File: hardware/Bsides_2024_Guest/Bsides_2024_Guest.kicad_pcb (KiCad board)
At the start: 2 copper layers, 134.5 x 129.5 mm, 53 parts, among them J1 Add_On, J2 Battery, J3 Battery, J4 OLED, J5 Serial_IN, J6 Serial_OUT, P1 USB_C_Plug_USB2.0, Q1 DMG3415U-7, SW1 ON, SW2 RESET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

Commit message: feat(Hw): Labels added
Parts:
- added kibuzzard-666B5A62: G***, kibuzzard-666B5A62, F.Cu at (179.3, 143.8)
- added kibuzzard-666B5A62: G***, kibuzzard-666B5A62, B.Cu at (70.0, 137.2)
- added kibuzzard-666B5A91: G***, kibuzzard-666B5A91, F.Cu at (181.1, 142.0)
- added kibuzzard-666B5A91: G***, kibuzzard-666B5A91, B.Cu at (71.7, 138.9)
- added kibuzzard-666B5AA1: G***, kibuzzard-666B5AA1, F.Cu at (182.7, 139.9)
- added kibuzzard-666B5AA1: G***, kibuzzard-666B5AA1, B.Cu at (68.4, 135.1)
- added kibuzzard-666B5BCA: G***, kibuzzard-666B5BCA, B.Cu at (142.8, 70.0)
- added kibuzzard-666B5C0A: G***, kibuzzard-666B5C0A, B.Cu at (142.0, 72.3)
- added kibuzzard-666B5C33: G***, kibuzzard-666B5C33, B.Cu at (144.6, 77.5)
- moved J3 2.95 mm to (115.4, 93.0)
- moved J2 2.79 mm to (132.9, 41.5)
- moved C5 1.26 mm to (104.3, 43.1)
- moved R6 0.25 mm to (102.4, 41.4)
- turned kibuzzard-666B5E08 to 135.5 degrees
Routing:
- net +BATT: track 47.0 -> 49.5 mm
- net GND: track 53.5 -> 55.1 mm
- net /VOUT: track 428.7 -> 429.8 mm
- net /PIN: track 108.3 -> 109.0 mm
- net Net-(D2-DIN): track 2.52 -> 1.98 mm

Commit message: feat(Hw): Update labels
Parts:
- removed kibuzzard-666B5EBB: G***, kibuzzard-666B5EBB
- added kibuzzard-666B5BCA: G***, kibuzzard-666B5BCA, B.Cu at (132.9, 91.0)
- added kibuzzard-666B5BCA: G***, kibuzzard-666B5BCA, B.Cu at (115.4, 43.3)
- added kibuzzard-666B5C0A: G***, kibuzzard-666B5C0A, B.Cu at (132.9, 43.0)
- added kibuzzard-666B5C0A: G***, kibuzzard-666B5C0A, B.Cu at (115.4, 91.2)
- added kibuzzard-666C662F: G***, kibuzzard-666C662F, B.Cu at (88.3, 71.7)

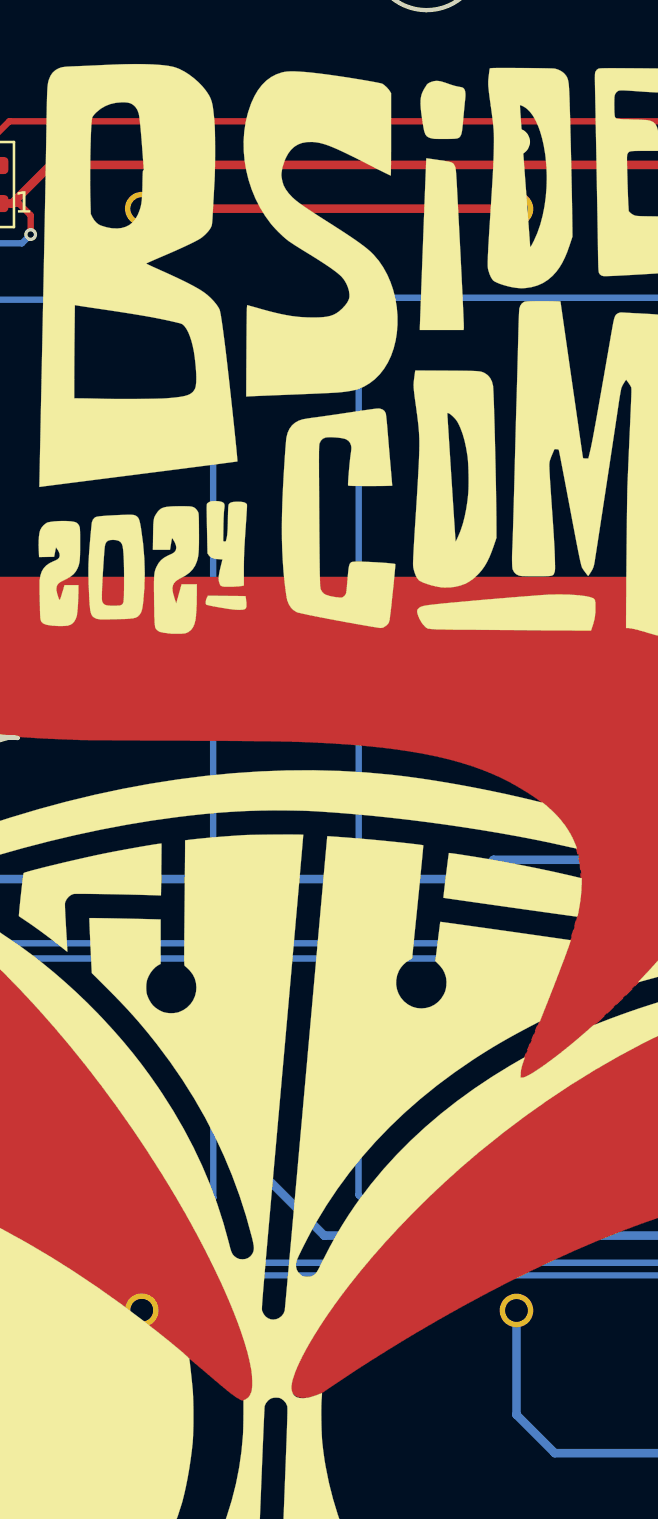
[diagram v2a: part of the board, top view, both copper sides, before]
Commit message: feat(Hw): Update labels
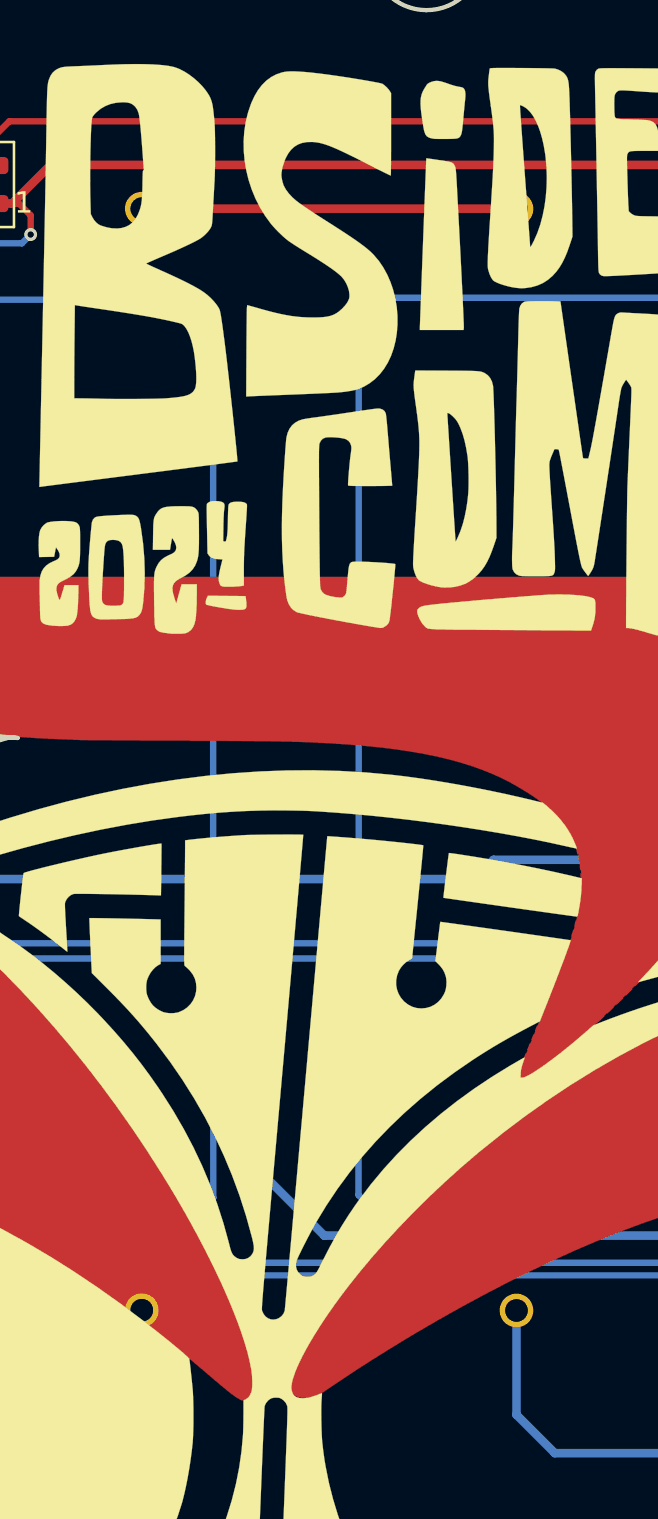
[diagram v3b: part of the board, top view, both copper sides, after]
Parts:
- removed the kibuzzard-666B5BCA at (115.4, 43.3)
- removed the kibuzzard-666B5C0A at (132.9, 43.0)
- moved kibuzzard-666B5BCA 5.99 mm to (132.9, 97.0)
- moved kibuzzard-666B5C0A 5.58 mm to (115.4, 96.7)
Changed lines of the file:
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@@
 		(attr through_hole)
 		(fp_line
-			(start -54.057905 -8.4906)
-			(end -54.057905 8.502)
+			(start 2.507895 -8.4906)
+			(end -54.057905 -8.4906)
 			(stroke
 				(width 0.1524)
@@
 		)
 		(fp_line
-			(start 2.507895 -8.490599)
-			(end -54.057905 -8.4906)
+			(start -54.057905 -8.4906)
+			(end -54.057905 8.502)
 			(stroke
 				(width 0.1524)
@@
 		(fp_line
 			(start 2.507895 8.502)
-			(end 2.507895 -8.490599)
+			(end 2.507895 -8.4906)
 			(stroke
 				(width 0.1524)
@@
 			(layer "B.SilkS")
 		)
-		(fp_circle
-			(center 3.142895 0)
-			(end 3.523895 0)
-			(stroke
-				(width 0.508)
-				(type solid)
-			)
-			(fill none)
-			(layer "B.SilkS")
-		)
-		(fp_circle
-			(center 3.142895 0)
-			(end 3.523895 0)
-			(stroke
-				(width 0.508)
-				(type solid)
-			)
-			(fill none)
-			(layer "F.SilkS")
-		)
 		(fp_line
 			(start 2.634895 -8.6176)
@@
 		(fp_line
 			(start 2.380895 -8.3636)
-			(end -53.930904 -8.3636)
+			(end -53.930905 -8.3636)
 			(stroke
 				(width 0.0254)
@@
 		)
 		(fp_line
-			(start -53.930904 -8.3636)
-			(end -53.930904 8.375)
+			(start -53.930905 -8.3636)
+			(end -53.930905 8.375)
 			(stroke
 				(width 0.0254)
@@
 		)
 		(fp_line
-			(start -53.930904 8.375)
+			(start -53.930905 8.375)
 			(end 2.380895 8.375)
 			(stroke
@@
 		(fp_circle
 			(center 0 1.905)
-			(end 0.381 1.905001)
+			(end 0.381 1.905)
 			(stroke
 				(width 0.508)
@@
 		)
 		(pad "2" thru_hole circle
-			(at -51.55001 0 90)
+			(at -51.550011 0 90)
 			(size 1.5748 1.5748)
 			(drill 1.0668)
@@
 		)
 	)
-	(footprint "kibuzzard-666B5C0A"
-		(layer "B.Cu")
-		(at 132.92 43.05)
-		(descr "Generated with KiBuzzard")
-		(tags "kb_params=eyJBbGlnbm1lbnRDaG9pY2UiOiAiQ2VudGVyIiwgIkNhcExlZnRDaG9pY2UiOiAiWyIsICJDYXBSaWdodENob2ljZSI6ICJdIiwgIkZvbnRDb21ib0JveCI6ICJVYnVudHVNb25vLUIiLCAiSGVpZ2h0Q3RybCI6IDAuMiwgIkxheWVyQ29tYm9Cb3giOiAiRi5TaWxrUyIsICJMaW5lU3BhY2luZ0N0cmwiOiAyLjAsICJNdWx0aUxpbmVUZXh0IjogIi0iLCAiUGFkZGluZ0JvdHRvbUN0cmwiOiAyLjAsICJQYWRkaW5nTGVmdEN0cmwiOiAyLjAsICJQYWRkaW5nUmlnaHRDdHJsIjogMi4wLCAiUGFkZGluZ1RvcEN0cmwiOiAyLjAsICJXaWR0aEN0cmwiOiAwLjZ9")
-		(property "Reference" "kibuzzard-666B5C0A"
-			(at 0 3.423482 360)
-			(layer "B.SilkS")
-			(hide yes)
-			(effects
-				(font
-					(size 0.001 0.001)
-					(thickness 0.15)
-				)
-				(justify mirror)
-			)
-		)
-		(property "Value" "G***"
-			(at 0 -3.423482 360)
-			(layer "B.SilkS")
-			(hide yes)
-			(effects
-				(font
-					(size 0.001 0.001)
-					(thickness 0.15)
-				)
-				(justify mirror)
-			)
-		)
-		(property "Footprint" ""
-			(at 0 0 360)
-			(layer "B.Fab")
-			(hide yes)
-			(effects
-				(font
-					(size 1.27 1.27)
-					(thickness 0.15)
-				)
-				(justify mirror)
-			)
-		)
-		(property "Datasheet" ""
-			(at 0 0 360)
-			(layer "B.Fab")
-			(hide yes)
-			(effects
-				(font
-					(size 1.27 1.27)
-					(thickness 0.15)
-				)
-				(justify mirror)
-			)
-		)
-		(property "Description" ""
-			(at 0 0 360)
-			(layer "B.Fab")
-			(hide yes)
-			(effects
-				(font
-					(size 1.27 1.27)
-					(thickness 0.15)
-				)
-				(justify mirror)
-			)
-		)
-		(attr board_only exclude_from_pos_files exclude_from_bom)
-		(fp_poly
-			(pts
-				(xy -0.226446 0.375482) (xy -0.501928 0.375482) (xy -0.501928 -0.375482) (xy -0.226446 -0.375482)
-				(xy 0.226446 -0.375482) (xy 0.226446 -0.1) (xy -0.226446 -0.1) (xy -0.226446 0.1) (xy 0.226446 0.1)
-				(xy 0.226446 -0.1) (xy 0.226446 -0.375482) (xy 0.501928 -0.375482) (xy 0.501928 0.375482) (xy 0.226446 0.375482)
-				(xy -0.226446 0.375482)
-			)
-			(stroke
-				(width 0)
-				(type solid)
-			)
-			(fill solid)
-			(layer "B.SilkS")
-		)
-	)
 	(footprint "Button_Switch_SMD:SW_SPST_TL3342"
 		(layer "B.Cu")
@@
 		(fp_arc
 			(start -2.4 3.300001)
-			(mid -2.450001 3.349982)
+			(mid -2.450001 3.349981)
 			(end -2.500001 3.299999)
 			(stroke
@@
 	(footprint "kibuzzard-666B5BCA"
 		(layer "B.Cu")
-		(at 132.95 91.03)
+		(at 132.94 97.02)
 		(descr "Generated with KiBuzzard")
 		(tags "kb_params=eyJBbGlnbm1lbnRDaG9pY2UiOiAiQ2VudGVyIiwgIkNhcExlZnRDaG9pY2UiOiAiWyIsICJDYXBSaWdodENob2ljZSI6ICJdIiwgIkZvbnRDb21ib0JveCI6ICJVYnVudHVNb25vLUIiLCAiSGVpZ2h0Q3RybCI6IDEuMCwgIkxheWVyQ29tYm9Cb3giOiAiRi5TaWxrUyIsICJMaW5lU3BhY2luZ0N0cmwiOiAxLjUsICJNdWx0aUxpbmVUZXh0IjogIisiLCAiUGFkZGluZ0JvdHRvbUN0cmwiOiAxLjAsICJQYWRkaW5nTGVmdEN0cmwiOiAyLjUsICJQYWRkaW5nUmlnaHRDdHJsIjogMi41LCAiUGFkZGluZ1RvcEN0cmwiOiAxLjAsICJXaWR0aEN0cmwiOiAxLjB9")
@@
 		(fp_line
 			(start 2.507895 8.502)
-			(end 2.507895 -8.490599)
-			(stroke
-				(width 0.1524)
-				(type solid)
-			)
-			(layer "B.SilkS")
-		)
-		(fp_line
-			(start 2.507895 -8.490599)
-			(end -54.057905 -8.4906)
+			(end 2.507895 -8.4906)
 			(stroke
 				(width 0.1524)
@@
 			(layer "B.SilkS")
 		)
-		(fp_circle
-			(center 3.142895 0)
-			(end 3.523895 0)
+		(fp_line
+			(start 2.507895 -8.4906)
+			(end -54.057905 -8.4906)
 			(stroke
-				(width 0.508)
+				(width 0.1524)
 				(type solid)
 			)
-			(fill none)
 			(layer "B.SilkS")
 		)
-		(fp_circle
-			(center 3.142895 0)
-			(end 3.523895 0)
-			(stroke
-				(width 0.508)
-				(type solid)
-			)
-			(fill none)
-			(layer "F.SilkS")
-		)
 		(fp_line
 			(start -54.184905 8.629)
@@
 		)
 		(fp_line
-			(start -53.930904 8.375)
+			(start -53.930905 8.375)
 			(end 2.380895 8.375)
 			(stroke
@@
 		)
 		(fp_line
-			(start -53.930904 -8.3636)
-			(end -53.930904 8.375)
+			(start -53.930905 -8.3636)
+			(end -53.930905 8.375)
 			(stroke
 				(width 0.0254)
@@
 		(fp_line
 			(start 2.380895 -8.3636)
-			(end -53.930904 -8.3636)
+			(end -53.930905 -8.3636)
 			(stroke
 				(width 0.0254)
@@
 		(fp_circle
 			(center 0 1.905)
-			(end 0.381 1.905001)
+			(end 0.381 1.905)
 			(stroke
 				(width 0.508)
@@
 		)
 		(pad "2" thru_hole circle
-			(at -51.55001 0 270)
+			(at -51.550011 0 270)
 			(size 1.5748 1.5748)
 			(drill 1.0668)
@@
 				(font
 					(size 0.001 0.001)
+					(thickness 0.15)
 				)
 				(justify mirror)
@@
 				(font
 					(size 0.001 0.001)
+					(thickness 0.15)
 				)
 				(justify mirror)
@@
 	(footprint "kibuzzard-666B5C0A"
 		(layer "B.Cu")
-		(at 115.42 91.15 180)
+		(at 115.39 96.73 180)
 		(descr "Generated with KiBuzzard")
 		(tags "kb_params=eyJBbGlnbm1lbnRDaG9pY2UiOiAiQ2VudGVyIiwgIkNhcExlZnRDaG9pY2UiOiAiWyIsICJDYXBSaWdodENob2ljZSI6ICJdIiwgIkZvbnRDb21ib0JveCI6ICJVYnVudHVNb25vLUIiLCAiSGVpZ2h0Q3RybCI6IDAuMiwgIkxheWVyQ29tYm9Cb3giOiAiRi5TaWxrUyIsICJMaW5lU3BhY2luZ0N0cmwiOiAyLjAsICJNdWx0aUxpbmVUZXh0IjogIi0iLCAiUGFkZGluZ0JvdHRvbUN0cmwiOiAyLjAsICJQYWRkaW5nTGVmdEN0cmwiOiAyLjAsICJQYWRkaW5nUmlnaHRDdHJsIjogMi4wLCAiUGFkZGluZ1RvcEN0cmwiOiAyLjAsICJXaWR0aEN0cmwiOiAwLjZ9")
@@
 			)
 			(stroke
-				(width 0)
-				(type solid)
-			)
-			(fill solid)
-			(layer "B.SilkS")
-		)
-	)
-	(footprint "kibuzzard-666B5BCA"
-		(layer "B.Cu")
-		(at 115.41 43.26 180)
-		(descr "Generated with KiBuzzard")
-		(tags "kb_params=eyJBbGlnbm1lbnRDaG9pY2UiOiAiQ2VudGVyIiwgIkNhcExlZnRDaG9pY2UiOiAiWyIsICJDYXBSaWdodENob2ljZSI6ICJdIiwgIkZvbnRDb21ib0JveCI6ICJVYnVudHVNb25vLUIiLCAiSGVpZ2h0Q3RybCI6IDEuMCwgIkxheWVyQ29tYm9Cb3giOiAiRi5TaWxrUyIsICJMaW5lU3BhY2luZ0N0cmwiOiAxLjUsICJNdWx0aUxpbmVUZXh0IjogIisiLCAiUGFkZGluZ0JvdHRvbUN0cmwiOiAxLjAsICJQYWRkaW5nTGVmdEN0cmwiOiAyLjUsICJQYWRkaW5nUmlnaHRDdHJsIjogMi41LCAiUGFkZGluZ1RvcEN0cmwiOiAxLjAsICJXaWR0aEN0cmwiOiAxLjB9")
-		(property "Reference" "kibuzzard-666B5BCA"
-			(at 0 3.733598 360)
-			(layer "B.SilkS")
-			(hide yes)
-			(effects
-				(font
-					(size 0.001 0.001)
-					(thickness 0.15)
-				)
-				(justify mirror)
-			)
-		)
-		(property "Value" "G***"
-			(at 0 -3.733598 360)
-			(layer "B.SilkS")
-			(hide yes)
-			(effects
-				(font
-					(size 0.001 0.001)
-					(thickness 0.15)
-				)
-				(justify mirror)
-			)
-		)
-		(property "Footprint" ""
-			(at 0 0 360)
-			(layer "B.Fab")
-			(hide yes)
-			(effects
-				(font
-					(size 1.27 1.27)
-					(thickness 0.15)
-				)
-				(justify mirror)
-			)
-		)
-		(property "Datasheet" ""
-			(at 0 0 360)
-			(layer "B.Fab")
-			(hide yes)
-			(effects
-				(font
-					(size 1.27 1.27)
-					(thickness 0.15)
-				)
-				(justify mirror)
-			)
-		)
-		(property "Description" ""
-			(at 0 0 360)
-			(layer "B.Fab")
-			(hide yes)
-			(effects
-				(font
-					(size 1.27 1.27)
-					(thickness 0.15)
-				)
-				(justify mirror)
-			)
-		)
-		(attr board_only exclude_from_pos_files exclude_from_bom)
-		(fp_poly
-			(pts
-				(xy -0.467706 0.685598) (xy -0.9317 0.685598) (xy -0.9317 -0.685598) (xy -0.467706 -0.685598) (xy 0.11804 -0.685598)
-				(xy 0.11804 -0.5) (xy -0.11804 -0.5) (xy -0.11804 -0.112472) (xy -0.467706 -0.112472) (xy -0.467706 0.112472)
-				(xy -0.11804 0.112472) (xy -0.11804 0.5) (xy 0.11804 0.5) (xy 0.11804 0.112472) (xy 0.467706 0.112472)
-				(xy 0.467706 -0.112472) (xy 0.11804 -0.112472) (xy 0.11804 -0.5) (xy 0.11804 -0.685598) (xy 0.467706 -0.685598)
-				(xy 0.9317 -0.685598) (xy 0.9317 0.685598) (xy 0.467706 0.685598) (xy -0.467706 0.685598)
-			)
-			(stroke

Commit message: feat(Hw):Update_Guest_SCH_Labels
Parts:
- F1: value 0.5A -> 0.75A
- SW2, SW4, SW6: value RESET -> ~
- SW3: value BOOT -> ~
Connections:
- net /GPIO16 renamed /TX
- net /GPIO17 renamed /RX
- net /GPIO4 renamed /RX1
- net /GPIO5 renamed /TX1

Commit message: feat(hw): add logos guest
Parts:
- removed the kibuzzard-666B5C0A at (115.4, 96.7)
- removed kibuzzard-666B5C33: G***, kibuzzard-666B5C33
- added G***: LOGO, LOGO, B.Cu at (123.3, 105.0)
- added G***: LOGO, LOGO, B.Cu at (111.5, 116.1)
- added REF**: OSHW-Logo_7.5x8mm_SilkScreen, Symbol:OSHW-Logo_7.5x8mm_SilkScreen, B.Cu at (94.5, 89.1)
- added kibuzzard-666C8E87: G***, kibuzzard-666C8E87, B.Cu at (123.4, 100.8)
- added kibuzzard-666C947A: G***, kibuzzard-666C947A, B.Cu at (144.6, 77.5)
- added kibuzzard-666C94C8: G***, kibuzzard-666C94C8, B.Cu at (115.4, 96.7)
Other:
- board text added: "4e6576657220676f6e6e612067 69766520796f752075700a4e65 76657220676f6e6e61206c6574 20796f7520646f776e0a4e6576 657220676f6e6e612072756e20 61726f756e6420616e64206465 7365727420796f75"
- board text added: "Aqui inicia el tour por latinoamerica Parce Wey Che"
- board text added: "Elige tu bando, rudo o tecnico?"
- board text added: "Lucharan de 2 a 3 caidas sin limite de tiempo!!"
